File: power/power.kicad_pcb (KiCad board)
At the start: 2 copper layers, 52 parts, among them J1 Conn_01x02_Female, J10 Conn_01x02_Female, J11 Conn_01x02_Female, J12 Conn_01x02_Female, J13 Conn_01x02_Female, J14 Conn_01x02_Female, J15 Conn_01x02_Female, J2 Barrel_jack, J3 CONN_02X03, J4 Conn_01x02_Female, J5 Conn_01x02_Female, J6 Conn_01x02_Female, J7 Conn_01x02_Female, J8 Conn_01x02_Female, J9 Conn_01x02_Female, Q1 BS170, Q2 BS170, Q3 BS170, Q5 BS170, Q6 BS170, Q7 BS170, U2 TPS2592xx, U3 ATMEGA16M1, U4 LP5907MFX-3_3_NOPB

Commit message: complete layout
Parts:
- moved J11 81.8 mm to (135.0, 119.3), turned to 0 degrees
- moved J10 76.0 mm to (140.2, 119.2), turned to 0 degrees
- moved J9 71.4 mm to (145.2, 119.2), turned to 0 degrees
- moved J8 67.1 mm to (180.6, 119.9), turned to 0 degrees
- moved J7 66.8 mm to (149.9, 119.3), turned to 0 degrees
- moved J1 66.0 mm to (160.4, 119.3), turned to 0 degrees
- moved J6 65.6 mm to (155.1, 119.3), turned to 0 degrees
- moved C6 42.5 mm to (165.2, 93.4)
- moved U4 42.5 mm to (160.0, 92.2)
- moved C7 40.7 mm to (159.7, 95.6), turned to 180 degrees
- moved J3 37.2 mm to (158.1, 62.0), turned to 0 degrees
- moved C1 19.0 mm to (185.1, 102.9), turned to 180 degrees
- moved R16 15.1 mm to (175.3, 78.9), turned to 90 degrees
- moved R14 14.6 mm to (174.5, 70.7), turned to 270 degrees
- moved R27 14.3 mm to (193.3, 107.2), turned to 0 degrees
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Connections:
- J3 pad 2: VCC -> +3V3
- U3 pad 13: /V2A -> Net-(U3-Pad13)
- U3 pad 14: /V1A -> Net-(U3-Pad14)
- U3 pad 16: /V3A -> Net-(U3-Pad16)
- U3 pad 17: /V3B -> Net-(U3-Pad17)
- U3 pad 2: Net-(U3-Pad2) -> /V2A
- U3 pad 22: Net-(U3-Pad22) -> /FET3B
- U3 pad 23: /FET2B -> /V3B
- U3 pad 24: /FET1B -> /FET2B
- U3 pad 25: Net-(U3-Pad25) -> /V2B
- U3 pad 26: /V1B -> /FET1B
- U3 pad 27: /V2B -> /V1B
- U3 pad 32: /FET3B -> /V1A
- U3 pad 6: /FET3A -> /V3A
- U3 pad 7: Net-(U3-Pad7) -> /FET3A
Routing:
- net /B1B+: track 0.00 -> 82.8 mm
- net GND: track 31.7 -> 113.8 mm, vias 8 -> 23
- net +3V3: track 0.00 -> 58.3 mm, vias 0 -> 3
- net +12V: track 0.00 -> 39.8 mm
- net /MISO: track 0.00 -> 33.8 mm, vias 0 -> 1
- net /MOSI: track 0.00 -> 33.4 mm, vias 0 -> 1
- net /FET3B: track 0.00 -> 31.4 mm
- net /B1B-: track 0.00 -> 29.7 mm
- net /B2B-: track 0.00 -> 26.0 mm
- net /V3B: track 0.00 -> 23.6 mm
- net /FET1B: track 0.00 -> 23.5 mm
- net /FET2B: track 0.00 -> 23.4 mm
- net /V1B: track 0.00 -> 19.4 mm
- net Net-(Q6-Pad3): track 0.00 -> 18.5 mm
- net /V2B: track 0.00 -> 17.7 mm
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- added copper zone on F.Cu, net +3V3
- removed copper zone on F.Cu, net +12V

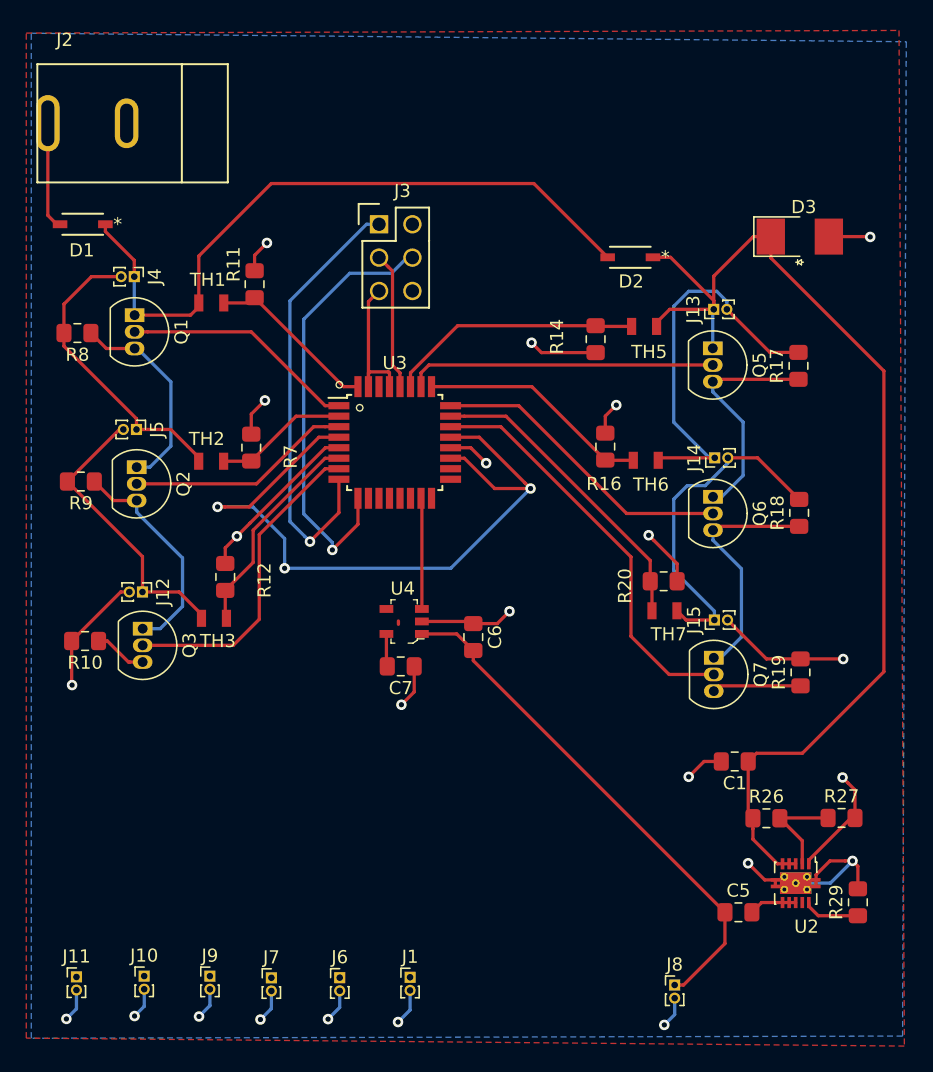
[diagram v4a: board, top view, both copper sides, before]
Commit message: power traces increased to 0.8
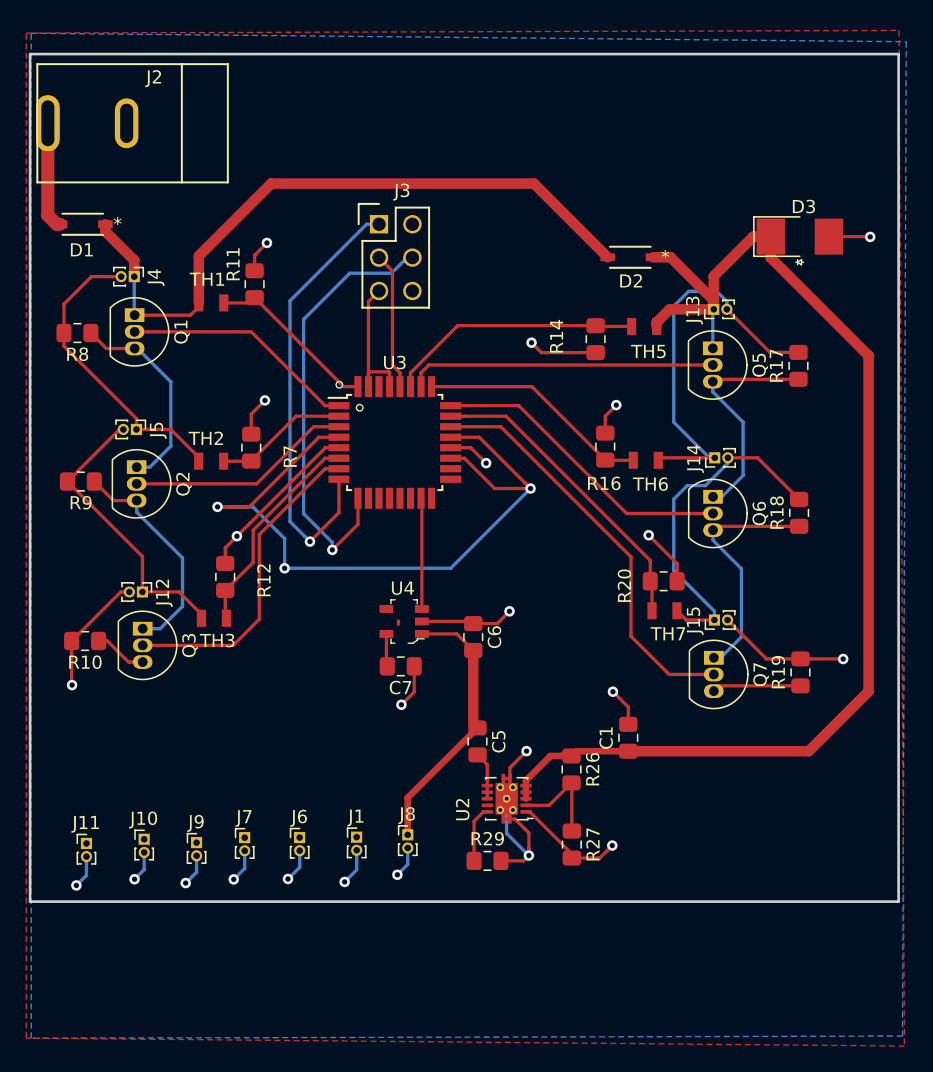
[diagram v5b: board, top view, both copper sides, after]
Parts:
- J2: value Barrel_jack -> Charging
- moved R29 28.4 mm to (166.3, 110.4), turned to 0 degrees
- moved C5 23.7 mm to (165.6, 101.3), turned to 270 degrees
- moved J8 23.3 mm to (160.2, 108.5)
- moved U2 22.9 mm to (167.8, 105.7), turned to 180 degrees
- moved R27 20.6 mm to (172.7, 109.2), turned to 270 degrees
- moved R26 15.3 mm to (172.7, 103.5), turned to 270 degrees
- moved J1 11.4 mm to (156.4, 108.6)
- moved J6 11.1 mm to (152.0, 108.7)
- moved J7 10.9 mm to (147.8, 108.7)
- moved J10 10.4 mm to (140.2, 108.8)
- moved J9 10.2 mm to (144.2, 109.1)
- moved J11 10.2 mm to (135.8, 109.1)
- moved C1 8.30 mm to (177.0, 101.1), turned to 90 degrees
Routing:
- net +12V: track 39.8 -> 20.8 mm
- net /B1B+: track 82.8 -> 90.8 mm
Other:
- board outline added: 66.1 x 64.5 mm
- net class 12V added: clearance 0.2, trace_width 0.8, via_dia 0.8, via_drill 0.4
- board text added: "+ -"

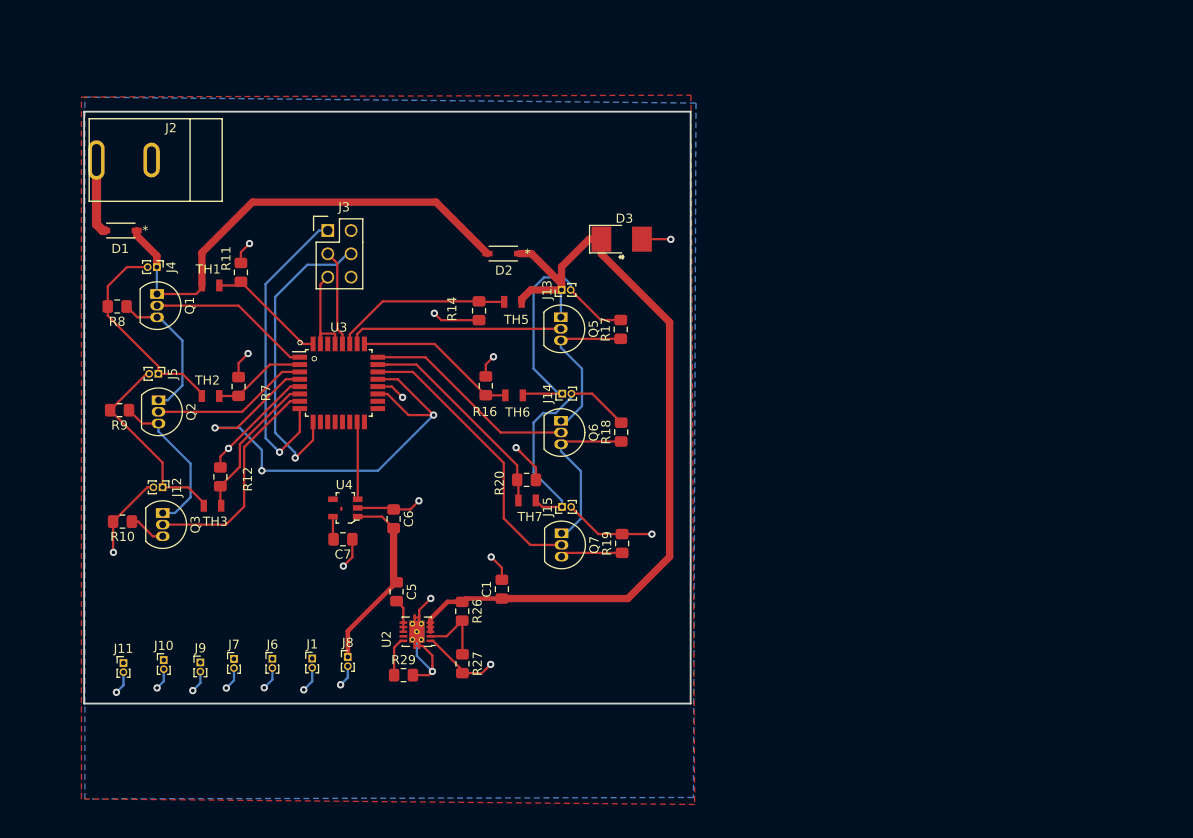
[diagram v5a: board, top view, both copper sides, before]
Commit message: layout complete other than missing recovery footprints
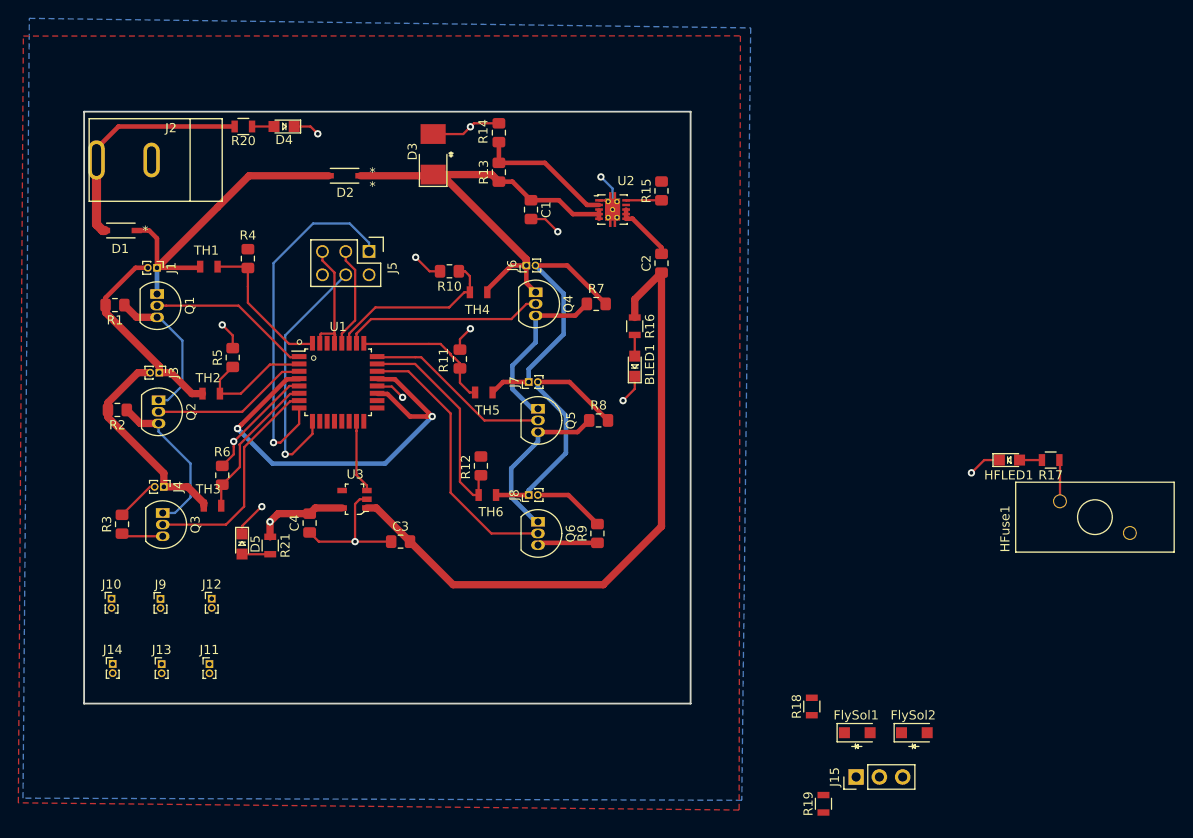
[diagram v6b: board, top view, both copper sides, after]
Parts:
- removed C5, C6, C7: 1uF, Capacitor_SMD:C_0805_2012Metric_Pad1.15x1.40mm_HandSolder
- removed Q7: BS170, Package_TO_SOT_THT:TO-92_Inline
- removed R26: 133, Resistor_SMD:R_0805_2012Metric_Pad1.15x1.40mm_HandSolder
- removed R27: 20, Resistor_SMD:R_0805_2012Metric_Pad1.15x1.40mm_HandSolder
- removed R29: 115K, Resistor_SMD:R_0805_2012Metric_Pad1.15x1.40mm_HandSolder
- removed TH7: Thermistor, footprints:Thermistor
- removed U4: LP5907MFX-3_3_NOPB, digikey-footprints:SOT-753
- added BLED1: LED_0805, footprints:LED_0805_OEM, F.Cu at (191.5, 76.8)
- added C2: 1uF, Capacitor_SMD:C_0805_2012Metric_Pad1.15x1.40mm_HandSolder, F.Cu at (194.4, 65.5)
- added C3: 1uF, Capacitor_SMD:C_0805_2012Metric_Pad1.15x1.40mm_HandSolder, F.Cu at (166.0, 95.9)
- added C4: 1uF, Capacitor_SMD:C_0805_2012Metric_Pad1.15x1.40mm_HandSolder, F.Cu at (156.1, 93.9)
- added D4: LED_0805_Red, footprints:LED_0805_OEM, F.Cu at (153.3, 50.6)
- added D5: LED_0805_Amber, footprints:LED_0805_OEM, F.Cu at (148.7, 96.1)
- added FlySol1: SS110LW, footprints:D_SOD-123W_OEM, F.Cu at (215.8, 116.7)
- added FlySol2: SS110LW, footprints:D_SOD-123W_OEM, F.Cu at (222.0, 116.7)
- added HFLED1: LED_0805, footprints:LED_0805_OEM, F.Cu at (232.4, 87.0)
- added HFuse1: 01530008Z, footprints:01530008Z, F.Cu at (230.5, 93.2)
- added Q4: BS170, Package_TO_SOT_THT:TO-92_Inline, F.Cu at (180.7, 68.7)
- added R1: 100, Resistor_SMD:R_0805_2012Metric_Pad1.15x1.40mm_HandSolder, F.Cu at (134.9, 70.1)
- added R13: 133, Resistor_SMD:R_0805_2012Metric_Pad1.15x1.40mm_HandSolder, F.Cu at (176.7, 55.6)
- added R15: 115K, Resistor_SMD:R_0805_2012Metric_Pad1.15x1.40mm_HandSolder, F.Cu at (194.4, 57.7)
- added R2: 100, Resistor_SMD:R_0805_2012Metric_Pad1.15x1.40mm_HandSolder, F.Cu at (135.1, 81.5)
- added R21: R_499, footprints:R_0805_OEM, F.Cu at (151.8, 96.3)
- added R3: 100, Resistor_SMD:R_0805_2012Metric_Pad1.15x1.40mm_HandSolder, F.Cu at (135.6, 94.0)
- added R4: 1.5K, Resistor_SMD:R_0805_2012Metric_Pad1.15x1.40mm_HandSolder, F.Cu at (149.4, 65.0)
- added R5: 1.5K, Resistor_SMD:R_0805_2012Metric_Pad1.15x1.40mm_HandSolder, F.Cu at (147.7, 75.8)
- added R6: 1.5K, Resistor_SMD:R_0805_2012Metric_Pad1.15x1.40mm_HandSolder, F.Cu at (146.6, 88.7)
- added TH4: Thermistor, footprints:Thermistor, F.Cu at (174.5, 68.7)
- added U1: ATMEGA16M1, footprints:TQFP-32_7x7mm_Pitch0.8mm, F.Cu at (159.2, 78.5)
- J15: value Conn_01x02_Female -> Conn_01x03_Male; footprint Connector_PinHeader_1.00mm:PinHeader_1x02_P1.00mm_Vertical -> Connector_PinHeader_2.54mm:PinHeader_1x03_P2.54mm_Vertical
- J2: value Charging -> Barrel_jack
- J3: value CONN_02X03 -> Conn_01x02_Female; footprint footprints:Pin_Header_Straight_2x03 -> Connector_PinHeader_1.00mm:PinHeader_1x02_P1.00mm_Vertical
- J5: value Conn_01x02_Female -> CONN_02X03; footprint Connector_PinHeader_1.00mm:PinHeader_1x02_P1.00mm_Vertical -> footprints:Pin_Header_Straight_2x03
- R10: value 100 -> 1.5K
- R14: value 1.5K -> 20
- R16, R20: value 1.5K -> R_499; footprint Resistor_SMD:R_0805_2012Metric_Pad1.15x1.40mm_HandSolder -> footprints:R_0805_OEM
- R17: value 100 -> R_499; footprint Resistor_SMD:R_0805_2012Metric_Pad1.15x1.40mm_HandSolder -> footprints:R_0805_OEM
- R18, R19: value 100 -> R_1K; footprint Resistor_SMD:R_0805_2012Metric_Pad1.15x1.40mm_HandSolder -> footprints:R_0805_OEM
- R7: value 1.5K -> 100
- U3: value ATMEGA16M1 -> LP5907MFX-3_3_NOPB; footprint footprints:TQFP-32_7x7mm_Pitch0.8mm -> digikey-footprints:SOT-753
- moved J13 59.7 mm to (140.0, 109.2), turned to 0 degrees
- moved J14 57.2 mm to (134.6, 109.2), turned to 0 degrees
- moved R8 53.9 mm to (187.6, 82.7), turned to 0 degrees
- moved R9 53.8 mm to (187.5, 95.0), turned to 90 degrees
- moved J6 51.0 mm to (179.7, 65.8), turned to 90 degrees
- moved U2 50.7 mm to (189.1, 59.7), turned to 0 degrees
- moved R20 49.4 mm to (148.9, 50.6)
- moved R17 49.0 mm to (236.9, 87.0), turned to 180 degrees
- moved J1 45.8 mm to (139.4, 66.0), turned to 270 degrees
- moved R10 44.9 mm to (171.3, 66.4)
- moved J7 44.1 mm to (180.0, 78.5), turned to 90 degrees
- moved J15 43.5 mm to (215.6, 121.5)
- moved C1 41.5 mm to (180.2, 59.7), turned to 270 degrees
- moved R7 40.0 mm to (187.3, 70.0), turned to 0 degrees
- moved R18 36.4 mm to (210.8, 113.9)
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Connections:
- J1 pad 1: +3V3 -> /B1A+
- J1 pad 2: GND -> /B1A-
- J12 pad 1: /B2A- -> +3V3
- J13 pad 1: /B1B+ -> +3V3
- J13 pad 2: /B1B- -> GND
- J14 pad 1: /B1B- -> +3V3
- J14 pad 2: /B2B- -> GND
- J15 pad 1: /B2B- -> /burn-wire
- J15 pad 2: GND -> /solenoid
- J3 pad 1: /MISO -> /B1A-
- J3 pad 2: +3V3 -> /B2A-
- J4 pad 1: /B1A+ -> /B2A-
- J4 pad 2: /B1A- -> GND
- J5 pad 1: /B1A- -> /MISO
- J5 pad 2: /B2A- -> +3V3
- J6 pad 1: +3V3 -> /B1B+
- J6 pad 2: GND -> /B1B-
- J7 pad 1: +3V3 -> /B1B-
- J7 pad 2: GND -> /B2B-
- J8 pad 1: +12V -> /B2B-
- Q5 pad 1: /B1B+ -> Net-(Q4-Pad3)
- Q5 pad 2: /FET1B -> /FET2B
- Q6 pad 2: /FET2B -> /FET3B
- R10 pad 1: Net-(Q3-Pad3) -> /V1B
- R11 pad 1: /V1A -> /V2B
- R12 pad 1: /V3A -> /V3B
- R14 pad 1: /V1B -> Net-(R13-Pad2)
- R16 pad 1: /V2B -> +12V
- R16 pad 2: GND -> Net-(BLED1-Pad2)
- R17 pad 1: Net-(Q5-Pad3) -> /12V_Switch
- R17 pad 2: /B1B- -> Net-(HFLED1-Pad2)
- R18 pad 1: Net-(Q6-Pad3) -> /solenoid
- R18 pad 2: /B2B- -> GND
- R19 pad 1: Net-(Q7-Pad3) -> /burn-wire
- R20 pad 1: /V3B -> /BAT+
- R20 pad 2: GND -> Net-(D4-Pad2)
- R7 pad 1: /V2A -> Net-(Q4-Pad3)
- R7 pad 2: GND -> /B1B-
- R8 pad 1: Net-(Q1-Pad3) -> Net-(Q5-Pad3)
- R8 pad 2: /B1A- -> /B2B-
- R9 pad 1: Net-(Q2-Pad3) -> Net-(Q6-Pad3)
- R9 pad 2: /B2A- -> GND
- TH5 pad 1: /B1B+ -> /B1B-
- TH5 pad 2: /V1B -> /V2B
- TH6 pad 1: /B1B- -> /B2B-
- TH6 pad 2: /V2B -> /V3B
- U2 pad 2: Net-(R26-Pad2) -> Net-(R13-Pad2)
- U3 pad 1: /FET1A -> +12V
- U3 pad 2: /V2A -> GND
- U3 pad 3: /FET2A -> /EN_LDO
- U3 pad 4: +3V3 -> Net-(U3-Pad4)
- U3 pad 5: GND -> +3V3
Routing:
- net +12V: track 20.8 -> 72.0 mm
- net /B1B+: track 90.8 -> 52.4 mm
- net GND: track 113.8 -> 83.4 mm, vias 23 -> 13
- net Net-(Q4-Pad3): track 0.00 -> 18.8 mm
- net /BAT+: track 8.22 -> 25.5 mm
- net /B1A+: track 52.6 -> 36.3 mm
- net Net-(R13-Pad2): track 0.00 -> 15.1 mm
- net Net-(Q6-Pad3): track 18.5 -> 6.58 mm
- net Net-(R26-Pad2): track 7.85 -> 0.00 mm
- net Net-(Q7-Pad3): track 6.77 -> 0.00 mm
- net /MOSI: track 33.4 -> 27.6 mm
- net /MISO: track 33.8 -> 39.0 mm
- net /12V_Switch: track 0.00 -> 4.52 mm
- net /V2A: track 10.2 -> 13.5 mm
- net Net-(C2-Pad2): track 3.64 -> 6.84 mm
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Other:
- board text added: "12V"
- board text added: "12V_Switch"
- board text added: "3.3V"
- board text added: "Charging"
